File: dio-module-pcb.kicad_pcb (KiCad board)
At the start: 2 copper layers, 82.5 x 101.6 mm, 76 parts, among them P1 RELAY_(JSM1A-12V-4), P2 RELAY_(JSM1A-12V-4), P3 RELAY_(JSM1A-12V-4), P4 RELAY_(JSM1A-12V-4), P5 RELAY_(JSM1A-12V-4), P6 RELAY_(JSM1A-12V-4), Q1 MMBT2222, Q10 MMBT2222, Q11 MMBT2222, Q12 MMBT2222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

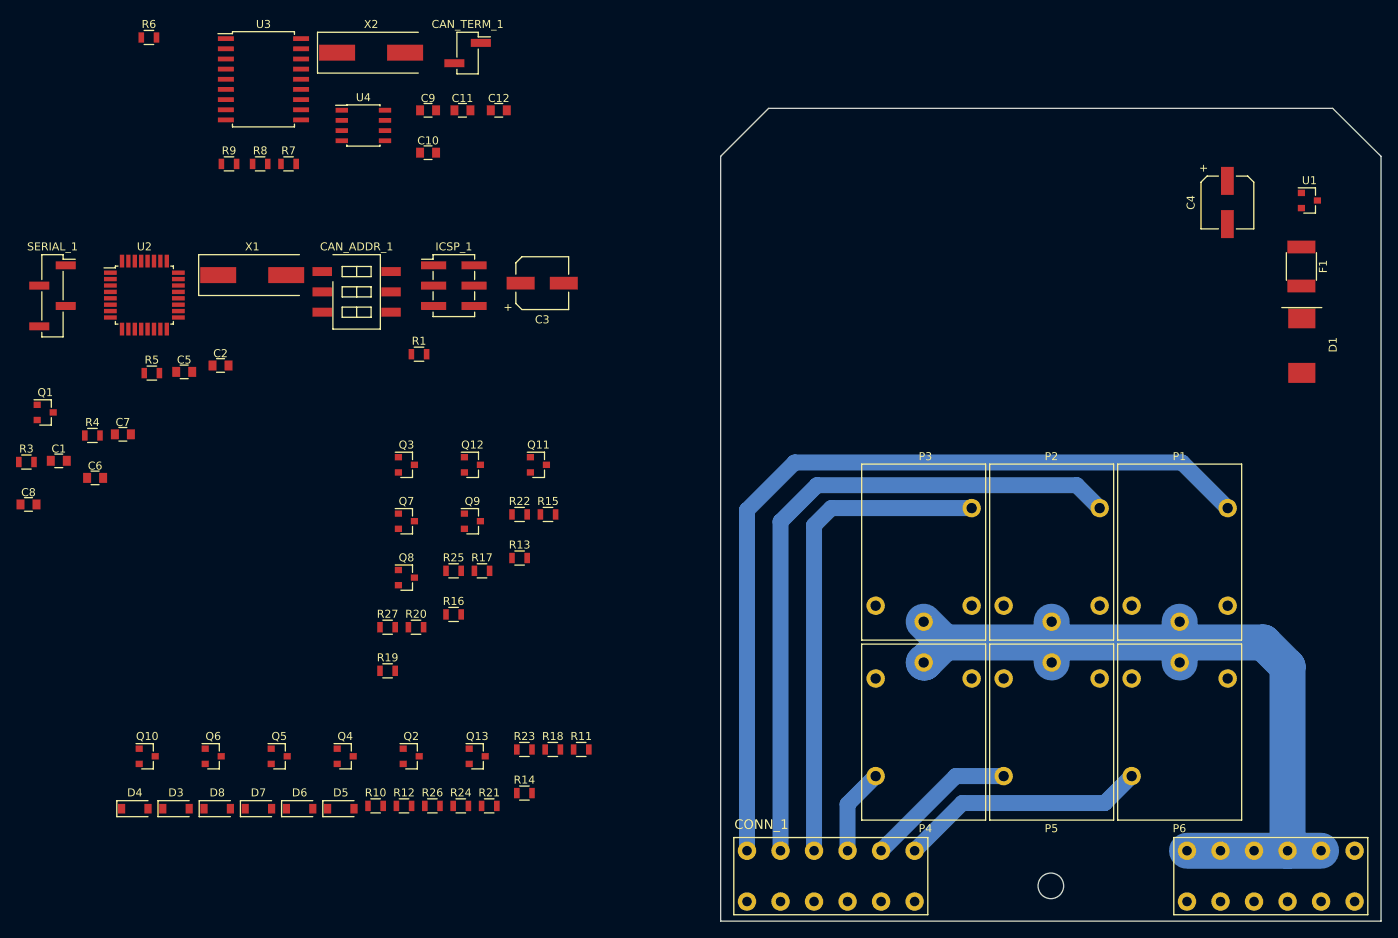
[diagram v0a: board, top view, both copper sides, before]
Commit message: - Finished circuit and PCB.
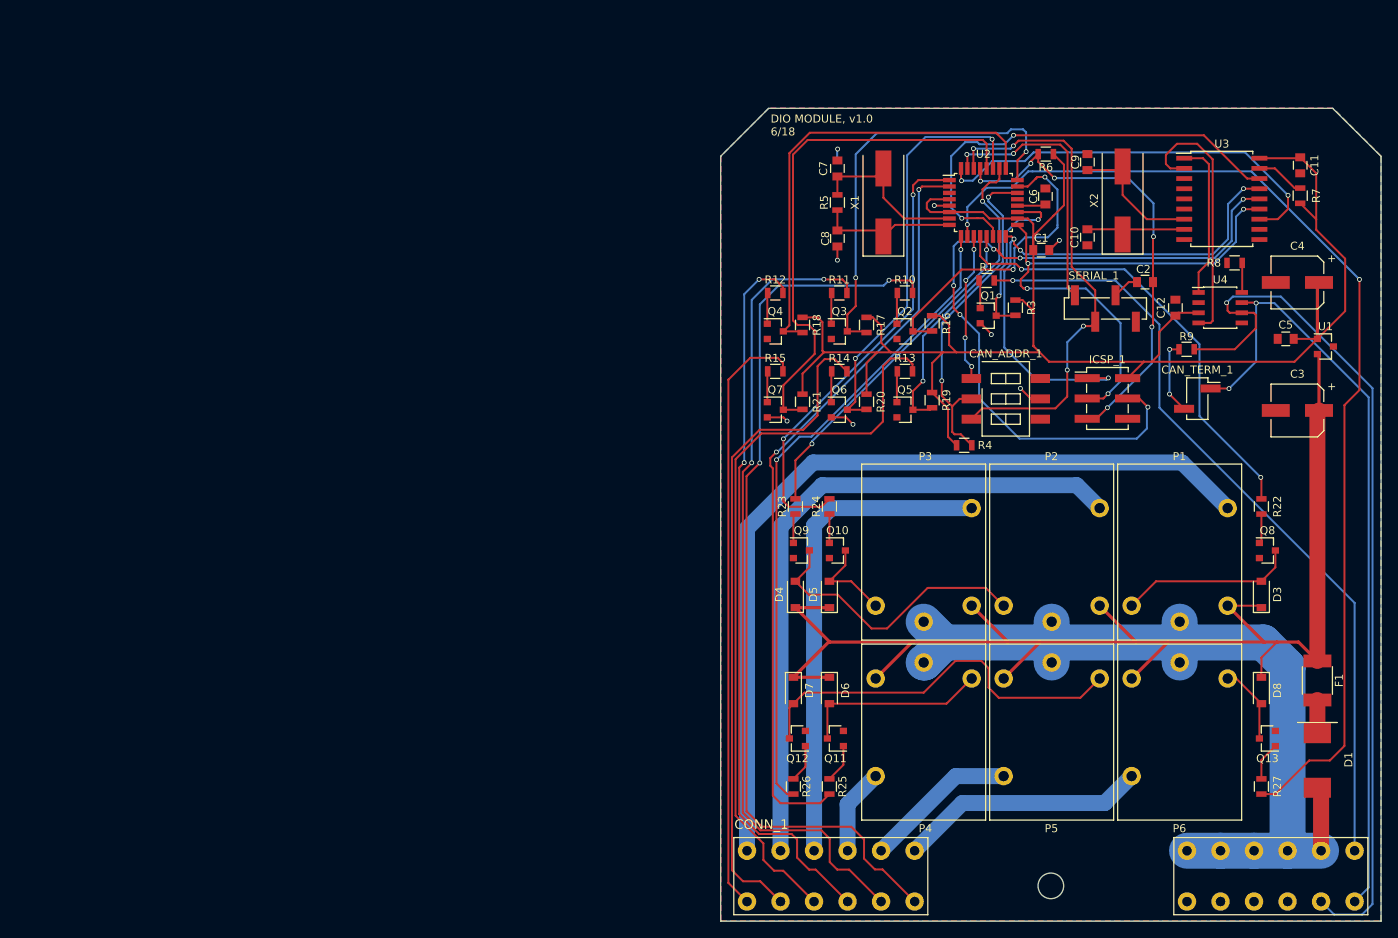
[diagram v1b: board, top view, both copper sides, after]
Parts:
- moved D3 138.3 mm to (172.8, 101.2), turned to 90 degrees
- moved C5 137.8 mm to (175.8, 69.3), turned to 180 degrees
- moved SERIAL_1 131.6 mm to (153.2, 65.5), turned to 90 degrees
- moved D8 131.4 mm to (172.8, 113.2), turned to 270 degrees
- moved R7 126.5 mm to (177.6, 51.4), turned to 90 degrees
- moved C1 125.6 mm to (145.2, 58.2)
- moved R3 125.1 mm to (142.0, 65.4), turned to 90 degrees
- moved C6 123.9 mm to (145.8, 51.5), turned to 90 degrees
- moved R8 122.4 mm to (169.4, 59.8)
- moved R9 121.9 mm to (163.4, 70.6), turned to 180 degrees
- moved U3 120.7 mm to (167.8, 51.8)
- moved Q1 118.5 mm to (138.6, 66.4)
- moved C2 116.0 mm to (158.2, 62.2), turned to 180 degrees
- moved R6 113.1 mm to (145.8, 46.2), turned to 180 degrees
- moved R27 111.0 mm to (172.8, 125.2), turned to 270 degrees
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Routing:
- net 5V: track 0.00 -> 216.8 mm
- net V_BATT_FU: track 0.00 -> 170.5 mm
- net DO5: track 0.00 -> 132.1 mm, vias 0 -> 2
- net DI0: track 0.00 -> 112.9 mm, vias 0 -> 2
- net CAN_LO: track 0.00 -> 110.7 mm, vias 0 -> 1
- net DI1: track 0.00 -> 102.5 mm, vias 0 -> 2
- net CAN_HI: track 0.00 -> 98.9 mm, vias 0 -> 2
- net Net-(CONN_1-PadB6): track 0.00 -> 98.8 mm, vias 0 -> 1
- net MOSI: track 0.00 -> 96.6 mm, vias 0 -> 6
- net DO3: track 0.00 -> 95.6 mm, vias 0 -> 2
- net DI3: track 0.00 -> 92.6 mm
- net DI2: track 0.00 -> 91.4 mm, vias 0 -> 2
- net DI4: track 0.00 -> 83.0 mm
- net DO4: track 0.00 -> 81.5 mm, vias 0 -> 2
- net DI5: track 0.00 -> 75.5 mm
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- added copper zone on B.Cu, net GND
- added copper zone on F.Cu, net GND
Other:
- net class Default: trace_width 0.4 -> 0.25; via_dia 1.5 -> 0.6; via_drill 0.6 -> 0.4
- board text added: "DIO MODULE, v1.0 6/18"
